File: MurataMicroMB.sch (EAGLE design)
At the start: 57 parts, among them CON1 C-2395, CON2 WM17143CT-ND, CON3 CON_MIL_10_ARM, CON4 C-2395, IC1 NC7SZ00M5XCT-ND, IC2 296-35164-1-ND, IC3 IC_LPC11U3XQFN33, IC4 AZ1117EH-3.3TRG1DICT-ND, Q1 1253-1168-1-ND, SW1 P-8073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

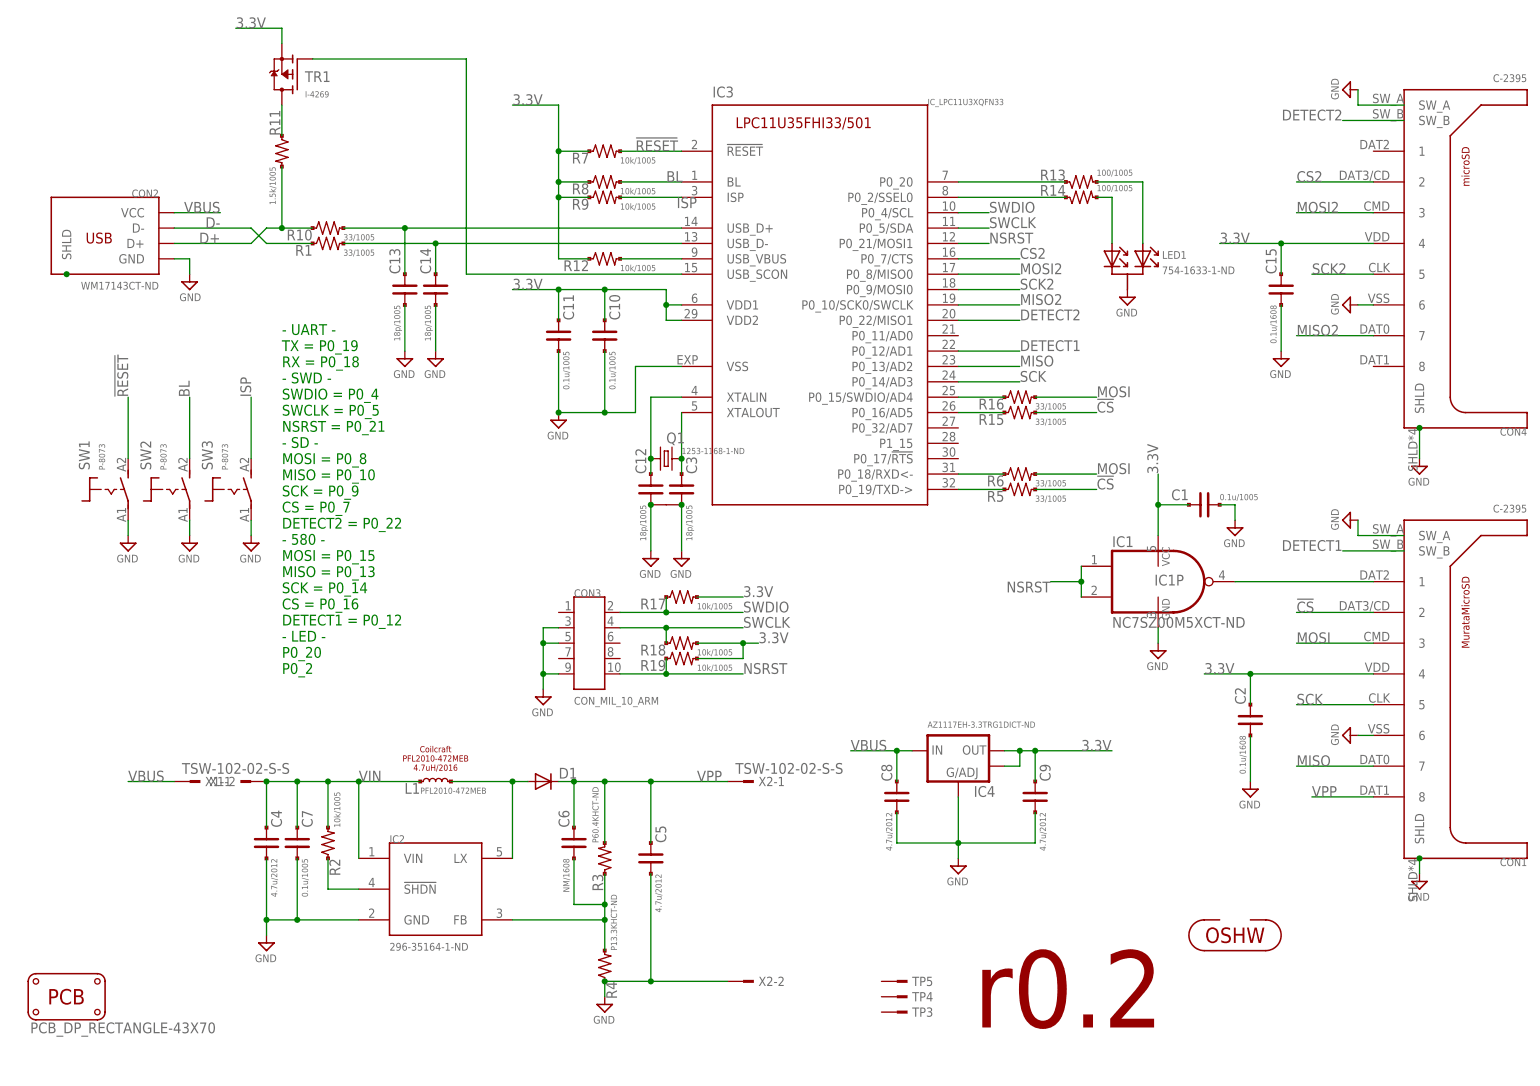
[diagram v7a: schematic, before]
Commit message: [ MB ] add R20/21; R7/8/9 move
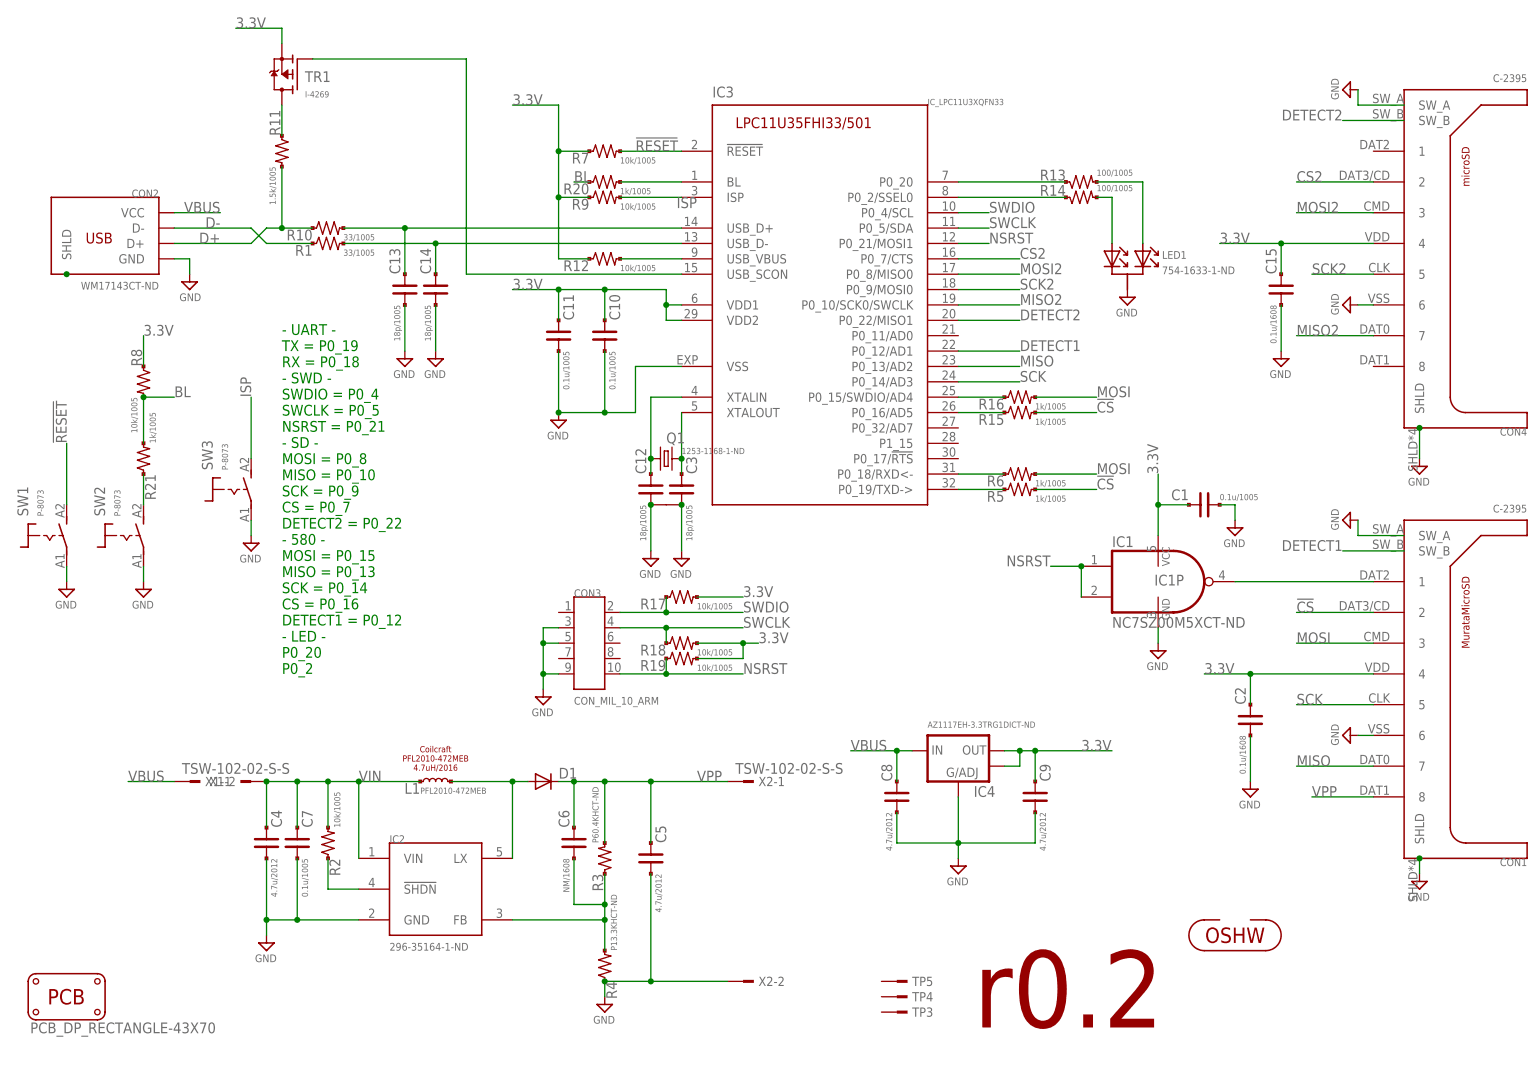
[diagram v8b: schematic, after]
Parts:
- added R20, R21: 1k/1005, mylib:R_US_PAD_PAD_1005
- R15, R16, R5, R6: value 33/1005 -> 1k/1005
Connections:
- new net N$19: R21.1, SW2.S
- new net N$21: IC3.BL, R20.2
- net BL: now also R20.1, R21.2; no longer IC3.BL, SW2.S
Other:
- moved on the sheet: R8, SW1, SW2
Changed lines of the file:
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@@
 <part name="C10" library="mylib" deviceset="C_PAD_PAD_" device="1005" value="0.1u/1005"/>
 <part name="C11" library="mylib" deviceset="C_PAD_PAD_" device="1005" value="0.1u/1005"/>
-<part name="R5" library="mylib" deviceset="R_US_PAD_PAD" device="_1005" value="33/1005"/>
-<part name="R6" library="mylib" deviceset="R_US_PAD_PAD" device="_1005" value="33/1005"/>
+<part name="R5" library="mylib" deviceset="R_US_PAD_PAD" device="_1005" value="1k/1005"/>
+<part name="R6" library="mylib" deviceset="R_US_PAD_PAD" device="_1005" value="1k/1005"/>
 <part name="R7" library="mylib" deviceset="R_US_PAD_PAD" device="_1005" value="10k/1005"/>
 <part name="R8" library="mylib" deviceset="R_US_PAD_PAD" device="_1005" value="10k/1005"/>
@@
 <part name="LED1" library="mylib" deviceset="LED_1SEG_A2K1" device="" value="754-1633-1-ND"/>
 <part name="SUPPLY24" library="mylib" deviceset="GND" device=""/>
-<part name="R15" library="mylib" deviceset="R_US_PAD_PAD" device="_1005" value="33/1005"/>
-<part name="R16" library="mylib" deviceset="R_US_PAD_PAD" device="_1005" value="33/1005"/>
+<part name="R15" library="mylib" deviceset="R_US_PAD_PAD" device="_1005" value="1k/1005"/>
+<part name="R16" library="mylib" deviceset="R_US_PAD_PAD" device="_1005" value="1k/1005"/>
 <part name="TP3" library="mylib" deviceset="TESTPAD" device="_F"/>
 <part name="TP4" library="mylib" deviceset="TESTPAD" device="_F"/>
@@
 <part name="R18" library="mylib" deviceset="R_US_PAD_PAD" device="_1005" value="10k/1005"/>
 <part name="R19" library="mylib" deviceset="R_US_PAD_PAD" device="_1005" value="10k/1005"/>
+<part name="R20" library="mylib" deviceset="R_US_PAD_PAD" device="_1005" value="1k/1005"/>
+<part name="R21" library="mylib" deviceset="R_US_PAD_PAD" device="_1005" value="1k/1005"/>
 </parts>
 <sheets>
@@
 <instance part="R6" gate="G$1" x="170.18" y="96.52"/>
 <instance part="R7" gate="G$1" x="101.6" y="149.86"/>
-<instance part="R8" gate="G$1" x="101.6" y="144.78"/>
+<instance part="R8" gate="G$1" x="25.4" y="111.76" rot="R270"/>
 <instance part="R9" gate="G$1" x="101.6" y="142.24"/>
 <instance part="Q1" gate="G$1" x="111.76" y="99.06" smashed="yes">
@@
 <instance part="R12" gate="G$1" x="101.6" y="132.08"/>
 <instance part="SUPPLY15" gate="GND" x="114.3" y="81.28"/>
-<instance part="SW1" gate="G$1" x="20.32" y="93.98"/>
-<instance part="SW2" gate="G$1" x="30.48" y="93.98"/>
+<instance part="SW1" gate="G$1" x="10.16" y="86.36"/>
+<instance part="SW2" gate="G$1" x="22.86" y="86.36"/>
 <instance part="SW3" gate="G$1" x="40.64" y="93.98"/>
-<instance part="SUPPLY16" gate="GND" x="22.86" y="83.82"/>
-<instance part="SUPPLY17" gate="GND" x="33.02" y="83.82"/>
+<instance part="SUPPLY16" gate="GND" x="12.7" y="76.2"/>
+<instance part="SUPPLY17" gate="GND" x="25.4" y="76.2"/>
 <instance part="SUPPLY18" gate="GND" x="43.18" y="83.82"/>
 <instance part="CON4" gate="G$1" x="241.3" y="132.08"/>
@@
 <instance part="R18" gate="G$1" x="114.3" y="68.58"/>
 <instance part="R19" gate="G$1" x="114.3" y="66.04"/>
+<instance part="R20" gate="G$1" x="101.6" y="144.78"/>
+<instance part="R21" gate="G$1" x="25.4" y="99.06" rot="R90"/>
 </instances>
 <busses>
@@
 <pinref part="SUPPLY16" gate="GND" pin="GND"/>
 <pinref part="SW1" gate="G$1" pin="P"/>
-<wire x1="22.86" y1="86.36" x2="22.86" y2="88.9" width="0.1524" layer="91"/>
+<wire x1="12.7" y1="78.74" x2="12.7" y2="81.28" width="0.1524" layer="91"/>
 </segment>
 <segment>
 <pinref part="SUPPLY17" gate="GND" pin="GND"/>
 <pinref part="SW2" gate="G$1" pin="P"/>
-<wire x1="33.02" y1="86.36" x2="33.02" y2="88.9" width="0.1524" layer="91"/>
+<wire x1="25.4" y1="78.74" x2="25.4" y2="81.28" width="0.1524" layer="91"/>
 </segment>
 <segment>
@@
 </segment>
 <segment>
-<wire x1="175.26" y1="78.74" x2="180.34" y2="78.74" width="0.1524" layer="91"/>
+<wire x1="175.26" y1="81.28" x2="180.34" y2="81.28" width="0.1524" layer="91"/>
 <pinref part="IC1" gate="A" pin="I0"/>
 <pinref part="IC1" gate="A" pin="I1"/>
-<wire x1="180.34" y1="81.28" x2="180.34" y2="78.74" width="0.1524" layer="91"/>
-<junction x="180.34" y="78.74"/>
-<wire x1="180.34" y1="78.74" x2="180.34" y2="76.2" width="0.1524" layer="91"/>
-<label x="175.26" y="78.74" size="1.778" layer="95" rot="R180"/>
+<junction x="180.34" y="81.28"/>
+<wire x1="180.34" y1="81.28" x2="180.34" y2="76.2" width="0.1524" layer="91"/>
+<label x="175.26" y="81.28" size="1.778" layer="95" rot="MR0"/>
 </segment>
 <segment>
@@
 <wire x1="93.98" y1="157.48" x2="93.98" y2="149.86" width="0.1524" layer="91"/>
 <pinref part="R9" gate="G$1" pin="1"/>
-<wire x1="93.98" y1="149.86" x2="93.98" y2="144.78" width="0.1524" layer="91"/>
-<wire x1="93.98" y1="144.78" x2="93.98" y2="142.24" width="0.1524" layer="91"/>
+<wire x1="93.98" y1="149.86" x2="93.98" y2="142.24" width="0.1524" layer="91"/>
 <wire x1="93.98" y1="142.24" x2="99.06" y2="142.24" width="0.1524" layer="91"/>
-<pinref part="R8" gate="G$1" pin="1"/>
-<wire x1="99.06" y1="144.78" x2="93.98" y2="144.78" width="0.1524" layer="91"/>
-<junction x="93.98" y="144.78"/>
 <pinref part="R7" gate="G$1" pin="1"/>
 <wire x1="99.06" y1="149.86" x2="93.98" y2="149.86" width="0.1524" layer="91"/>
@@
 <junction x="124.46" y="68.58"/>
 <label x="127" y="68.58" size="1.778" layer="95"/>
+</segment>
+<segment>
+<wire x1="25.4" y1="119.38" x2="25.4" y2="114.3" width="0.1524" layer="91"/>
+<pinref part="R8" gate="G$1" pin="1"/>
+<label x="25.4" y="119.38" size="1.778" layer="95"/>
 </segment>
 </net>
@@
 <net name="BL" class="0">
 <segment>
-<pinref part="IC3" gate="G$1" pin="BL"/>
 <pinref part="R8" gate="G$1" pin="2"/>
-<wire x1="114.3" y1="144.78" x2="104.14" y2="144.78" width="0.1524" layer="91"/>
-<label x="111.76" y="144.78" size="1.778" layer="95"/>
-</segment>
-<segment>
-<wire x1="33.02" y1="109.22" x2="33.02" y2="99.06" width="0.1524" layer="91"/>
-<pinref part="SW2" gate="G$1" pin="S"/>
-<label x="33.02" y="109.22" size="1.778" layer="95" rot="R90"/>
+<wire x1="25.4" y1="109.22" x2="25.4" y2="101.6" width="0.1524" layer="91"/>
+<pinref part="R21" gate="G$1" pin="2"/>
+<label x="30.48" y="109.22" size="1.778" layer="95"/>
+<wire x1="25.4" y1="109.22" x2="30.48" y2="109.22" width="0.1524" layer="91"/>
+<junction x="25.4" y="109.22"/>
+</segment>
+<segment>
+<pinref part="R20" gate="G$1" pin="1"/>
+<wire x1="99.06" y1="144.78" x2="96.52" y2="144.78" width="0.1524" layer="91"/>
+<label x="96.52" y="144.78" size="1.778" layer="95"/>
 </segment>
 </net>
@@
 </segment>
 <segment>
-<wire x1="22.86" y1="99.06" x2="22.86" y2="109.22" width="0.1524" layer="91"/>
+<wire x1="12.7" y1="91.44" x2="12.7" y2="101.6" width="0.1524" layer="91"/>
 <pinref part="SW1" gate="G$1" pin="S"/>
-<label x="22.86" y="109.22" size="1.778" layer="95" rot="R90"/>
+<label x="12.7" y="101.6" size="1.778" layer="95" rot="R90"/>
 </segment>
 </net>
@@
 </segment>
 </net>
+<net name="N$21" class="0">
+<segment>
+<pinref part="R20" gate="G$1" pin="2"/>
+<pinref part="IC3" gate="G$1" pin="BL"/>
+<wire x1="104.14" y1="144.78" x2="114.3" y2="144.78" width="0.1524" layer="91"/>
+</segment>
+</net>
+<net name="N$19" class="0">
+<segment>
+<pinref part="SW2" gate="G$1" pin="S"/>
+<pinref part="R21" gate="G$1" pin="1"/>
+<wire x1="25.4" y1="96.52" x2="25.4" y2="91.44" width="0.1524" layer="91"/>
+</segment>
+</net>
